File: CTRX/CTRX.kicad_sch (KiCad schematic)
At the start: 33 parts, among them J1 USB_B_Micro, J2 SMA_CONNECTOR, J3 Conn_02x05_Odd_Even, U1 nRF52820-QDxx, U2 NRF21540-QDAA-R7, U3 USBLC6-2SC6, U4 ME6211C33M5, Y1 32MHz

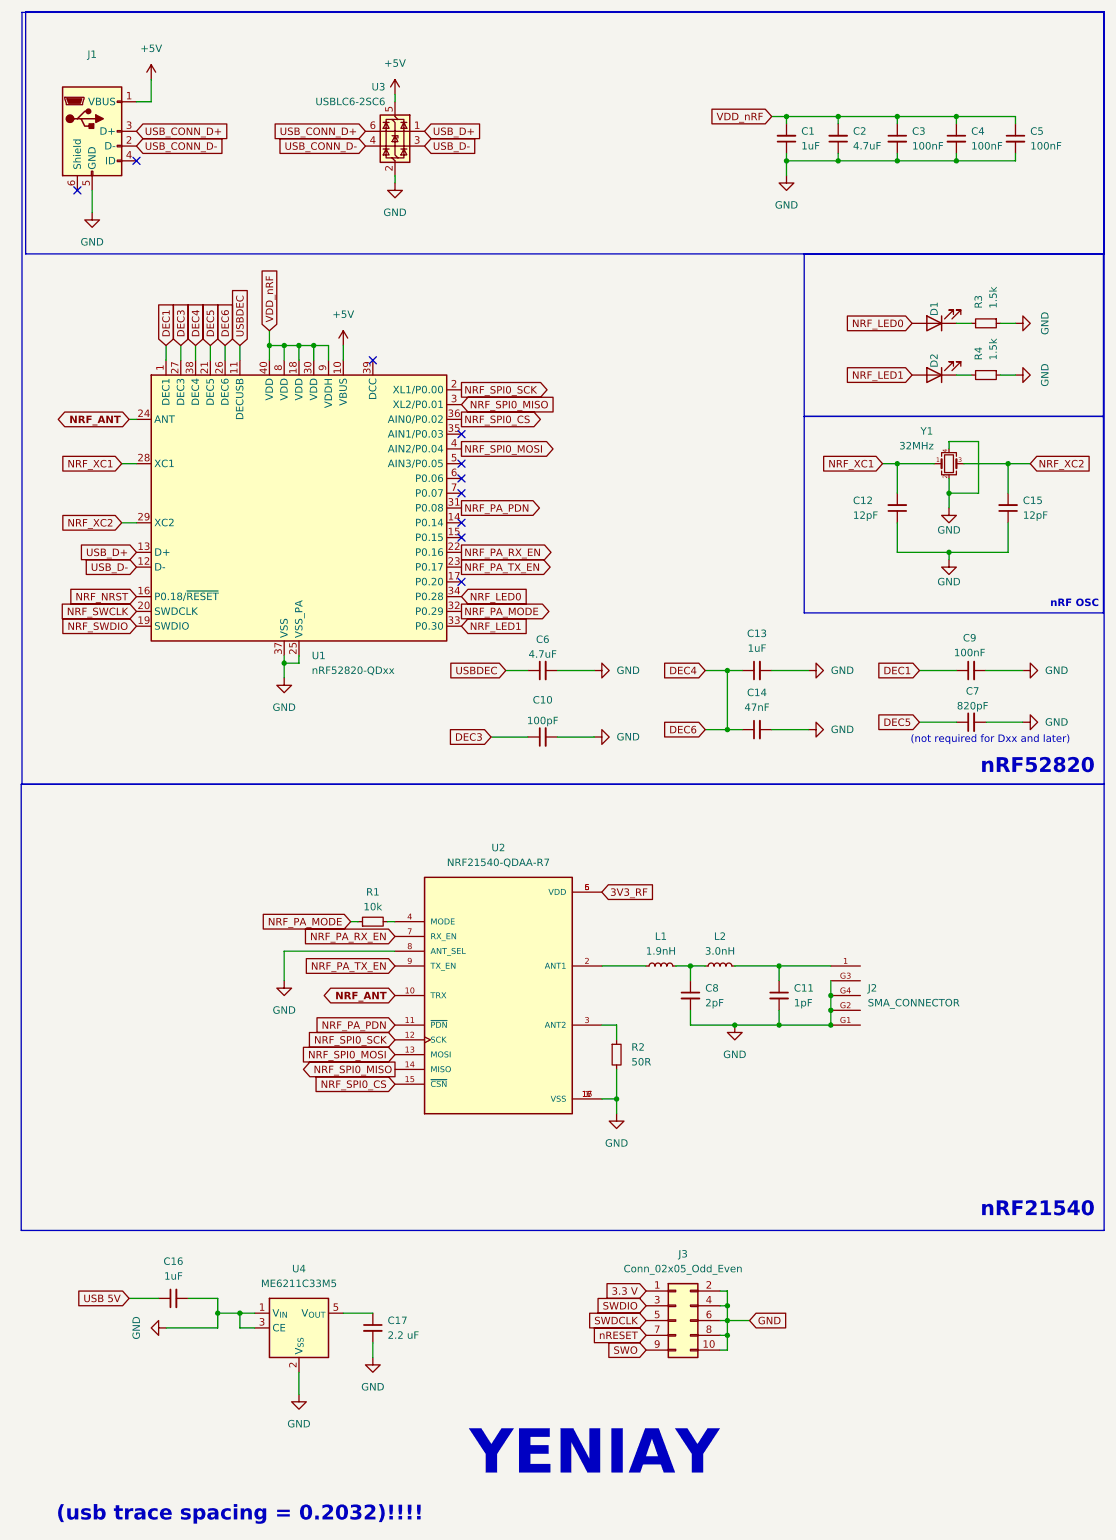
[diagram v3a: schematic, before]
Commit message: Pin baglantilari duzenlendi, C12/C15 12pF yapildi, nrf anten pinine 1 pF kapasitor eklendi, 2x5 debug connector ve regulator eklendi.
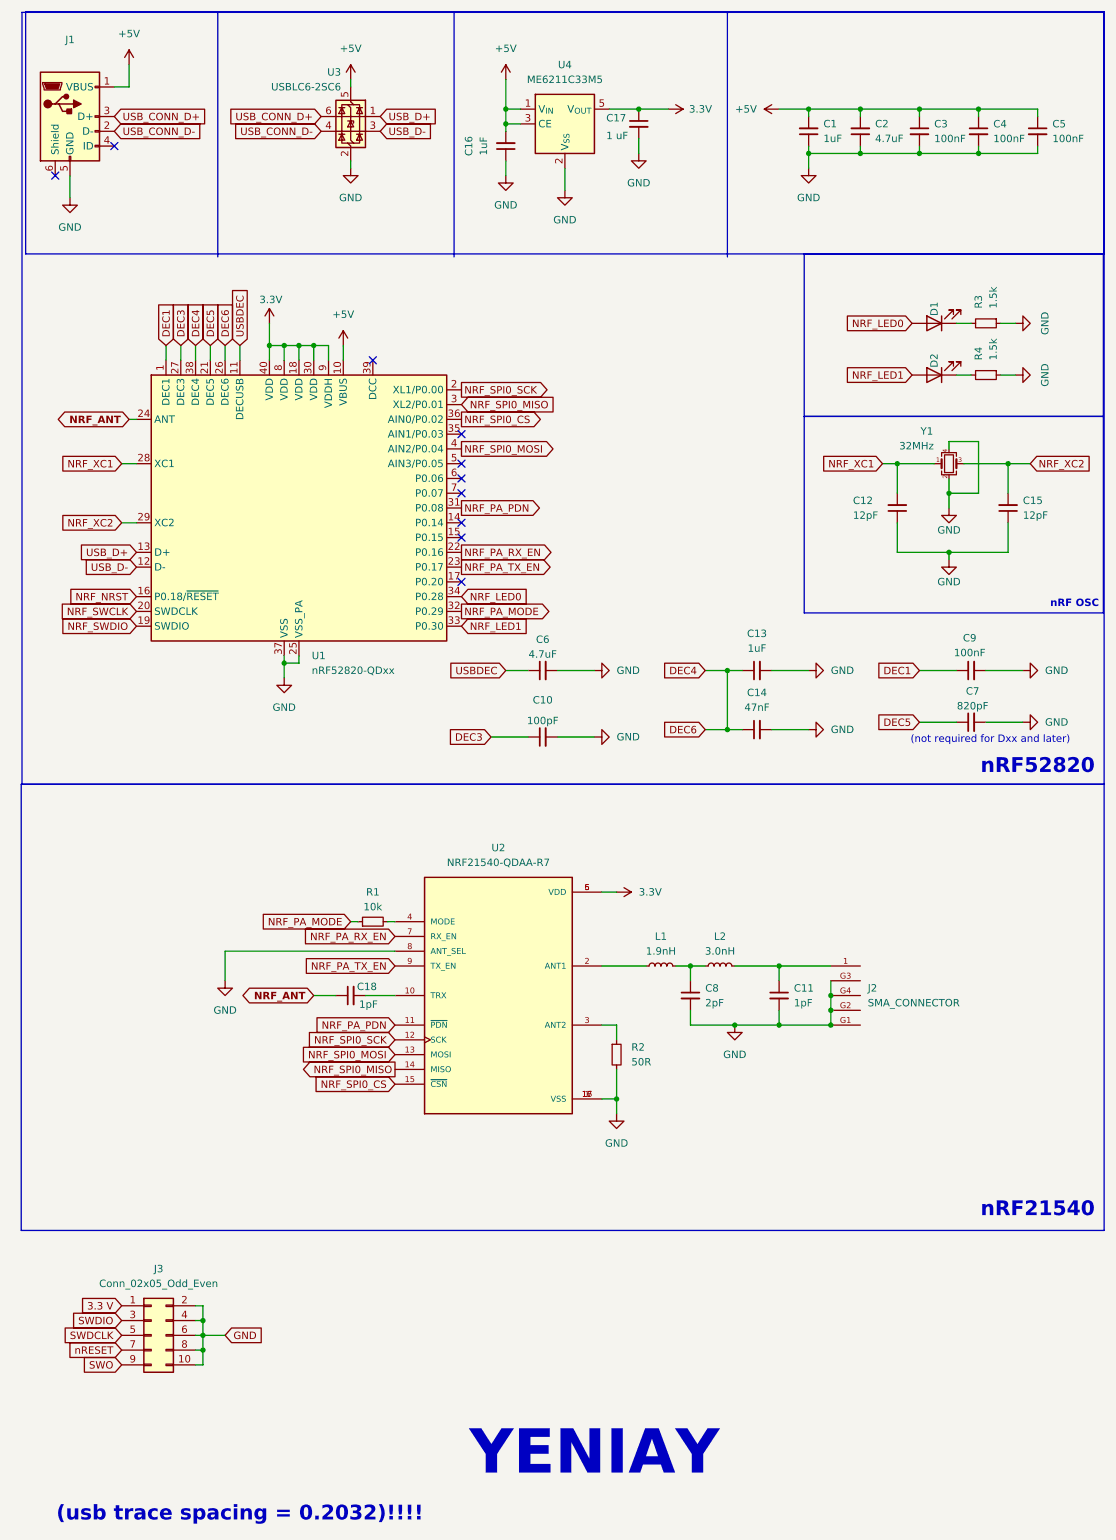
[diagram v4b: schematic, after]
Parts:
- added C18: 1pF, Capacitor_SMD:C_0201_0603Metric, symbol Device:C_Small
- C17: value 2.2 uF -> 1 uF
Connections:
- net 3V3_RF is gone; now on net 3.3V: U2.5 (VDD), U2.6 (VDD)
- net USB 5V is gone; now on net GND: C16.1
- net +5V: now also C1.2, C16.2, C2.2, C3.1, C4.1, C5.1, U4.1 (V_{IN}), U4.3 (CE)
- net GND: no longer C16.2, U4.1 (V_{IN}), U4.3 (CE)
- net NRF_ANT: now also C18.1; no longer U2.10 (TRX)
- net 3.3V: now reaches C17.1, U4.5 (V_{OUT})
- net 3.3V: now also U1.18 (VDD), U1.30 (VDD), U1.40 (VDD), U1.8 (VDD), U1.9 (VDDH)
- removed net VDD_nRF: C1.2, C2.2, C3.1, C4.1, C5.1, U1.18 (VDD), U1.30 (VDD), U1.40 (VDD), U1.8 (VDD), U1.9 (VDDH)
- new net: C18.2, U2.10 (TRX)
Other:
- moved on the sheet: C1, C16, C17, C2, C3, C4, C5, J1, J3, U3, U4

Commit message: schematic upgraded
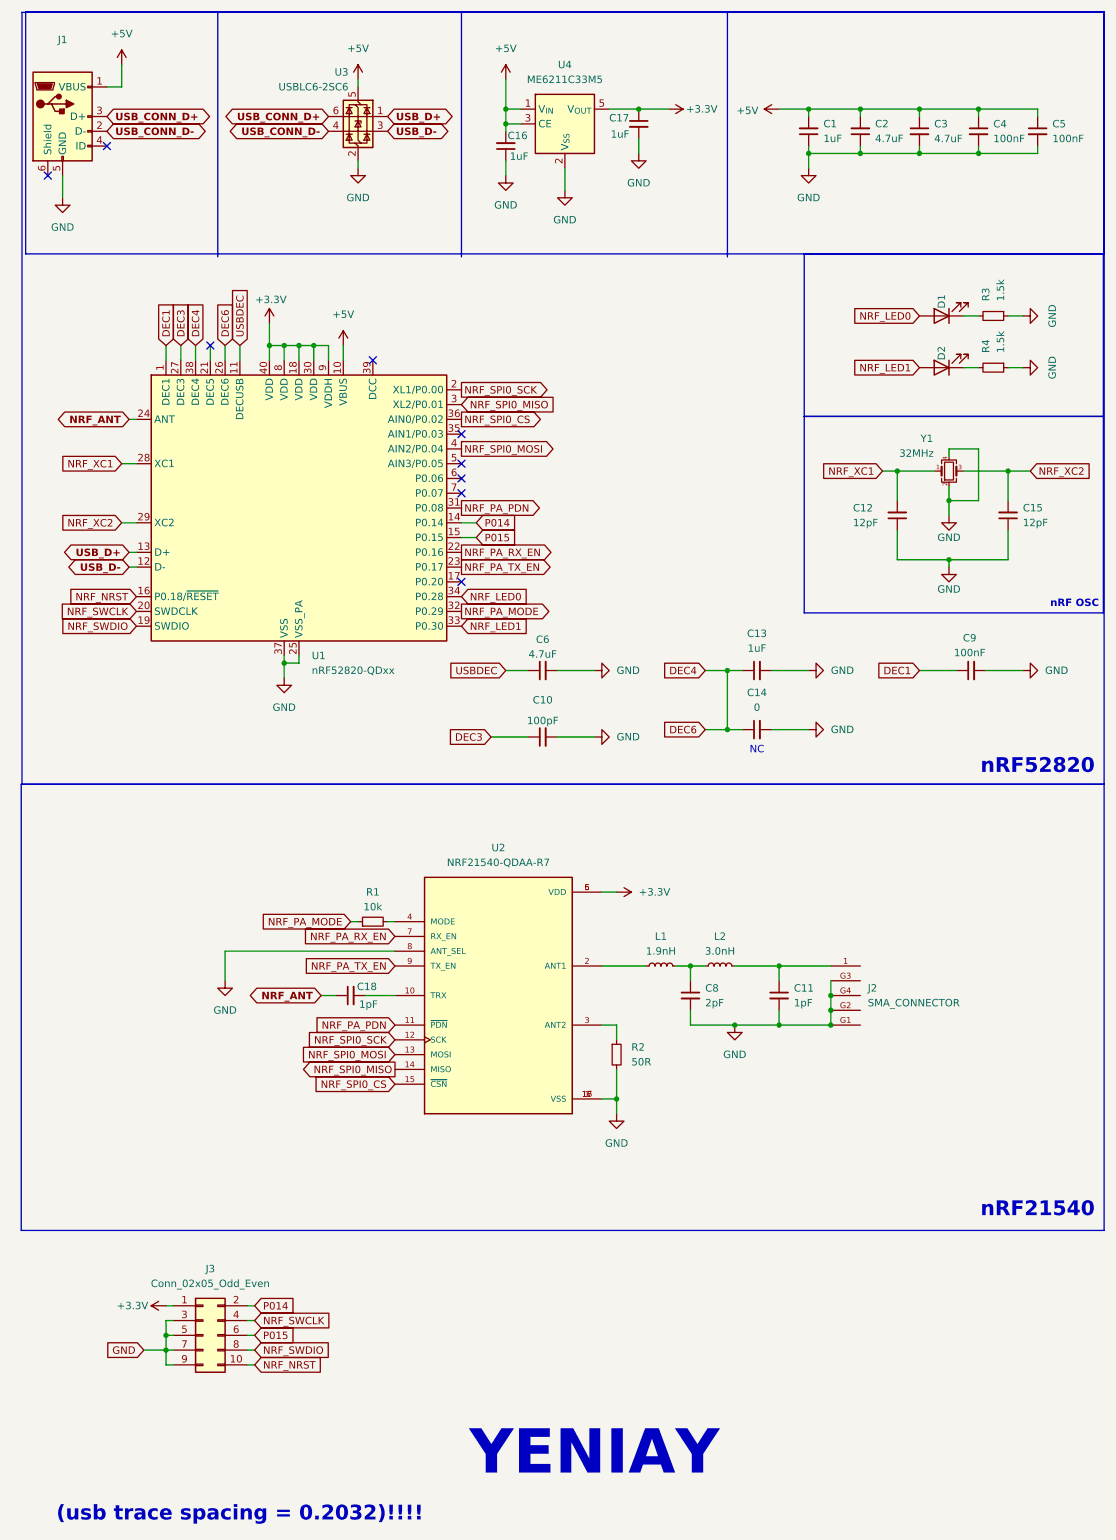
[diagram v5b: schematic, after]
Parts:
- removed C7: 820pF, Capacitor_SMD:C_0201_0603Metric, symbol Device:C_Small
- C14: value 47nF -> 0
- C17: value 1 uF -> 1uF
- C3: value 100nF -> 4.7uF
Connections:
- net 3.3V is gone; now on net +3.3V: C17.1, U1.18 (VDD), U1.30 (VDD), U1.40 (VDD), U1.8 (VDD), U1.9 (VDDH), U2.5 (VDD), U2.6 (VDD), U4.5 (V_{OUT})
- net SWDCLK is gone; now on net GND: J3.5 (Pin_5)
- net SWDIO is gone; now on net GND: J3.3 (Pin_3)
- net SWO is gone; now on net GND: J3.9 (Pin_9)
- net nRESET is gone; now on net GND: J3.7 (Pin_7)
- net GND: no longer J3.10 (Pin_10), J3.2 (Pin_2), J3.4 (Pin_4), J3.6 (Pin_6), J3.8 (Pin_8)
- net NRF_NRST: now also J3.10 (Pin_10)
- net NRF_SWCLK: now also J3.4 (Pin_4)
- net NRF_SWDIO: now also J3.8 (Pin_8)
- net P014: now reaches U1.14 (P0.14)
- net P014: now also J3.2 (Pin_2)
- net P015: now reaches U1.15 (P0.15)
- net P015: now also J3.6 (Pin_6)
- net 3.3 V renamed +3.3V
- net DEC5: no longer names the net of U1.21 (DEC5)
- no-connect marks 10 -> 9
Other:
- note added: "NC"
- note removed: "(not required for Dxx and later)"
- moved on the sheet: C12, C15, D1, D2, J1, J3, R3, R4, U3, Y1

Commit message: schematic updated
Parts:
- removed J1: USB_B_Micro, symbol Connector:USB_B_Micro
- added J4: USB-AM-S-X-X-TH, USB-AM-S-X-X-TH:SAMTEC_USB-AM-S-X-X-TH, symbol USB-AM-S-X-X-TH:USB-AM-S-X-X-TH
- C16, C17: footprint (none) -> Capacitor_SMD:C_0402_1005Metric
- C3: footprint Capacitor_SMD:C_0201_0603Metric -> Capacitor_SMD:C_0603_1608Metric
- J3: footprint (none) -> Connector_IDC:IDC-Header_2x05_P2.54mm_Vertical
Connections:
- net +5V: now also J4.01 (VCC)
- net GND: now also J4.04 (GND)
- net USB_CONN_D+: now also J4.03 (D+)
- net USB_CONN_D-: now also J4.02 (D-)
- new net: J4.S1 (SHIELD), J4.S2 (SHIELD)
- no-connect marks 9 -> 8
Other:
- moved on the sheet: C1, C10, C13, C14, C16, C17, C2, C3, C4, C5, C6, C9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

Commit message: sma edge added
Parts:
- removed J2: SMA_CONNECTOR, LPRS_SMA_CONNECTOR:LPRS_SMA_CONNECTOR, symbol SMA_CONNECTOR:SMA_CONNECTOR
- added J1: CON-SMA-EDGE-S, SMA-EDGE:RFSOLUTIONS_CON-SMA-EDGE-S, symbol CON-SMA-EDGE-S:CON-SMA-EDGE-S
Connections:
- net GND: now also J1.G1, J1.G2, J1.G3, J1.G4
- net at C11.1, L2.2: now also J1.1
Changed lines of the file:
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@@
 	)
 	(junction
-		(at 152.4 185.42)
-		(diameter 0)
-		(color 0 0 0 0)
-	)
-	(junction
 		(at 143.51 187.96)
 		(diameter 0)
@@
 	)
 	(junction
-		(at 152.4 182.88)
-		(diameter 0)
-		(color 0 0 0 0)
-	)
-	(junction
 		(at 60.96 71.12)
 		(diameter 0)
@@
 	)
 	(junction
-		(at 152.4 187.96)
-		(diameter 0)
-		(color 0 0 0 0)
-	)
-	(junction
 		(at 58.42 125.73)
 		(diameter 0)
@@
 	(wire
 		(pts
-			(xy 152.4 185.42) (xy 152.4 187.96)
-		)
-		(stroke
-			(width 0)
-			(type default)
-		)
-	)
-	(wire
-		(pts
 			(xy 125.73 177.8) (xy 128.27 177.8)
 		)
@@
 	(wire
 		(pts
-			(xy 152.4 182.88) (xy 152.4 185.42)
-		)
-		(stroke
-			(width 0)
-			(type default)
-		)
-	)
-	(wire
-		(pts
 			(xy 128.27 177.8) (xy 130.81 177.8)
 		)
@@
 	(wire
 		(pts
-			(xy 152.4 180.34) (xy 152.4 182.88)
+			(xy 152.4 180.34) (xy 152.4 187.96)
 		)
 		(stroke
@@
 	)
 	(symbol
-		(lib_id "SMA_CONNECTOR:SMA_CONNECTOR")
-		(at 154.94 177.8 0)
-		(mirror y)
-		(unit 1)
-		(exclude_from_sim no)
-		(in_bom yes)
-		(on_board yes)
-		(dnp no)
-		(fields_autoplaced yes)
-		(property "Reference" "J2"
-			(at 158.75 181.6099 0)
-			(effects
-				(font
-					(size 1.27 1.27)
-				)
-				(justify right)
-			)
-		)
-		(property "Value" "SMA_CONNECTOR"
-			(at 158.75 184.1499 0)
-			(effects
-				(font
-					(size 1.27 1.27)
-				)
-				(justify right)
-			)
-		)
-		(property "Footprint" "LPRS_SMA_CONNECTOR:LPRS_SMA_CONNECTOR"
-			(at 154.94 172.72 0)
-			(effects
-				(font
-					(size 1.27 1.27)
-				)
-				(justify bottom)
-				(hide yes)
-			)
-		)
-		(property "Datasheet" ""
-			(at 154.94 180.34 0)
-			(effects
-				(font
-					(size 1.27 1.27)
-				)
-				(hide yes)
-			)
-		)
-		(property "Description" ""
-			(at 154.94 180.34 0)
-			(effects
-				(font
-					(size 1.27 1.27)
-				)
-				(hide yes)
-			)
-		)
-		(property "MF" "LPRS"
-			(at 154.94 173.99 0)
-			(effects
-				(font
-					(size 1.27 1.27)
-				)
-				(justify bottom)
-				(hide yes)
-			)
-		)
-		(property "MAXIMUM_PACKAGE_HEIGHT" "8.3 mm"
-			(at 154.94 172.72 0)
-			(effects
-				(font
-					(size 1.27 1.27)
-				)
-				(justify bottom)
-				(hide yes)
-			)
-		)
-		(property "Package" "None"
-			(at 154.94 173.99 0)
-			(effects
-				(font
-					(size 1.27 1.27)
-				)
-				(justify bottom)
-				(hide yes)
-			)
-		)
-		(property "Price" "None"
-			(at 154.94 173.99 0)
-			(effects
-				(font
-					(size 1.27 1.27)
-				)
-				(justify bottom)
-				(hide yes)
-			)
-		)
-		(property "Check_prices" "https://www.snapeda.com/parts/SMA%20CONNECTOR/LPRS/view-part/?ref=eda"
-			(at 154.94 172.72 0)
-			(effects
-				(font
-					(size 1.27 1.27)
-				)
-				(justify bottom)
-				(hide yes)
-			)
-		)
-		(property "STANDARD" "Manufacturer Recommendations"
-			(at 154.94 172.72 0)
-			(effects
-				(font
-					(size 1.27 1.27)
-				)
-				(justify bottom)
-				(hide yes)
-			)
-		)
-		(property "PARTREV" "1.3"
-			(at 154.94 173.99 0)
-			(effects
-				(font
-					(size 1.27 1.27)
-				)
-				(justify bottom)
-				(hide yes)
-			)
-		)
-		(property "SnapEDA_Link" "https://www.snapeda.com/parts/SMA%20CONNECTOR/LPRS/view-part/?ref=snap"
-			(at 154.94 172.72 0)
-			(effects
-				(font
-					(size 1.27 1.27)
-				)
-				(justify bottom)
-				(hide yes)
-			)
-		)
-		(property "MP" "SMA CONNECTOR"
-			(at 154.94 173.99 0)
-			(effects
-				(font
-					(size 1.27 1.27)
-				)
-				(justify bottom)
-				(hide yes)
-			)
-		)
-		(property "Description_1" "\nRF Coaxial Straight SMA Connector\n"
-			(at 154.94 172.72 0)
-			(effects
-				(font
-					(size 1.27 1.27)
-				)
-				(justify bottom)
-				(hide yes)
-			)
-		)
-		(property "Availability" "In Stock"
-			(at 154.94 173.99 0)
-			(effects
-				(font
-					(size 1.27 1.27)
-				)
-				(justify bottom)
-				(hide yes)
-			)
-		)
-		(property "MANUFACTURER" "LPRS"
-			(at 154.94 173.99 0)
-			(effects
-				(font
-					(size 1.27 1.27)
-				)
-				(justify bottom)
-				(hide yes)
-			)
-		)
-		(pin "G1"
-		)
-		(pin "G2"
-		)
-		(pin "1"
-		)
-		(pin "G3"
-		)
-		(pin "G4"
-		)
-		(instances
-			(project "CTRX"
-				(path "/cc5d7565-c489-4dd3-a56f-c087f99b94a5"
-					(reference "J2")
-					(unit 1)
-				)
-			)
-		)
-	)
-	(symbol
 		(lib_id "NRF21540-QDAA-R7:NRF21540-QDAA-R7")
 		(at 95.25 182.88 0)
@@
 					(unit 1)
 				)
+			)
+		)
+	)
+	(symbol
+		(lib_id "CON-SMA-EDGE-S:CON-SMA-EDGE-S")
+		(at 154.94 180.34 0)
+		(mirror y)
+		(unit 1)
+		(exclude_from_sim no)
+		(in_bom yes)
+		(on_board yes)
+		(dnp no)
+		(property "Reference" "J1"
+			(at 160.02 180.5941 0)
+			(effects
+				(font
+					(size 1.27 1.27)
+				)
+				(justify right)
+			)
+		)
+		(property "Value" "CON-SMA-EDGE-S"
+			(at 160.02 178.0541 0)
+			(effects
+				(font
+					(size 1.27 1.27)
+				)
+				(justify right)
+			)
+		)
+		(property "Footprint" "SMA-EDGE:RFSOLUTIONS_CON-SMA-EDGE-S"
+			(at 154.94 180.34 0)
+			(effects
+				(font
+					(size 1.27 1.27)
+				)
+				(justify bottom)
+				(hide yes)
+			)
+		)
+		(property "Datasheet" ""
+			(at 154.94 180.34 0)
+			(effects
+				(font
+					(size 1.27 1.27)
+				)
+				(hide yes)
+			)
+		)
+		(property "Description" ""
+			(at 154.94 180.34 0)
+			(effects
+				(font
+					(size 1.27 1.27)
+				)
+				(hide yes)
+			)
+		)
+		(property "MF" "RF Solutions"
+			(at 154.94 180.34 0)
+			(effects
+				(font
+					(size 1.27 1.27)
+				)
+				(justify bottom)
+				(hide yes)
+			)
+		)
+		(property "MAXIMUM_PACKAGE_HEIGHT" "6.35mm"
+			(at 154.94 180.34 0)
+			(effects
+				(font
+					(size 1.27 1.27)
+				)
+				(justify bottom)
+				(hide yes)
+			)
+		)
+		(property "Package" "None"
+			(at 154.94 180.34 0)
+			(effects
+				(font
+					(size 1.27 1.27)
+				)
+				(justify bottom)
+				(hide yes)
+			)
+		)
+		(property "Price" "None"
+			(at 154.94 180.34 0)
+			(effects
+				(font
+					(size 1.27 1.27)
+				)
+				(justify bottom)
+				(hide yes)
+			)
+		)
+		(property "Check_prices" "https://www.snapeda.com/parts/CON-SMA-EDGE-S/RF+Solutions/view-part/?ref=eda"
+			(at 154.94 180.34 0)
+			(effects
+				(font
+					(size 1.27 1.27)
+				)
+				(justify bottom)
+				(hide yes)
+			)
+		)
+		(property "STANDARD" "Manufacturer Recommendations"
+			(at 154.94 180.34 0)
+			(effects
+				(font
+					(size 1.27 1.27)
+				)
+				(justify bottom)
+				(hide yes)
+			)
+		)
+		(property "PARTREV" "1"
+			(at 154.94 180.34 0)
+			(effects
+				(font
+					(size 1.27 1.27)
+				)
+				(justify bottom)
+				(hide yes)
+			)
+		)
+		(property "SnapEDA_Link" "https://www.snapeda.com/parts/CON-SMA-EDGE-S/RF+Solutions/view-part/?ref=snap"
+			(at 154.94 180.34 0)
+			(effects
+				(font
+					(size 1.27 1.27)
+				)
+				(justify bottom)
+				(hide yes)
+			)
+		)
+		(property "MP" "CON-SMA-EDGE-S"
+			(at 154.94 180.34 0)
+			(effects
+				(font
+					(size 1.27 1.27)
+				)
+				(justify bottom)
+				(hide yes)
+			)
+		)
+		(property "Description_1" "\nSMA Connector Jack, Female Socket - Board Edge, End Launch Solder\n"
+			(at 154.94 180.34 0)
+			(effects
+				(font
+					(size 1.27 1.27)
+				)
+				(justify bottom)
+				(hide yes)
+			)
+		)
+		(property "Availability" "In Stock"
+			(at 154.94 180.34 0)
+			(effects
+				(font
+					(size 1.27 1.27)
+				)
+				(justify bottom)
+				(hide yes)
+			)
+		)
+		(property "MANUFACTURER" "RF Solutions"
+			(at 154.94 180.34 0)
+			(effects
+				(font
+					(size 1.27 1.27)
+				)
+				(justify bottom)
+				(hide yes)
+			)
+		)
+		(pin "G1"
+		)
+		(pin "G2"
+		)
+		(pin "G4"
+		)
+		(pin "1"
+		)
+		(pin "G3"
+		)
+		(instances
+			(project ""
+				(path "/cc5d7565-c489-4dd3-a56f-c087f99b94a5"
+					(reference "J1")
+					(unit 1)
+				)
